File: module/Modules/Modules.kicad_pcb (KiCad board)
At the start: 2 copper layers, 165.5 x 77.7 mm, 27 parts, among them J1 Conn_01x04_MountingPin, J2 Conn_01x04, J3 Conn_01x04, J4 Conn_01x04, U1 COM-09032, U2 LTC4316xDD, U3 24LC32, U7 24AA02-OT, U9 ADS1115IDGS

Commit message: update
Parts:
- removed JP3: SolderJumper_3_Open, Jumper:SolderJumper-3_P1.3mm_Open_RoundedPad1.0x1.5mm_NumberLabels
- removed R2, R4: R, PCM_Resistor_SMD_AKL:R_0805_2012Metric_Pad1.15x1.40mm_HandSolder
- removed U2: LTC4316xDD, Package_SO:MSOP-10_3x3mm_P0.5mm
- removed U3: 24LC32, Package_SO:SOIC-8_3.9x4.9mm_P1.27mm
- added J1: Conn_01x04_MountingPin, Connector_JST:JST_SH_BM04B-SRSS-TB_1x04-1MP_P1.00mm_Vertical, F.Cu at (253.9, 111.3)
- added JP2: int, Jumper:SolderJumper-2_P1.3mm_Open_RoundedPad1.0x1.5mm, B.Cu at (262.6, 89.3)
- JP1: value SolderJumper_3_Open -> WP; footprint Jumper:SolderJumper-3_P1.3mm_Open_RoundedPad1.0x1.5mm_NumberLabels -> Jumper:SolderJumper-2_P1.3mm_Open_RoundedPad1.0x1.5mm; moved to B.Cu
- R1: value R -> 100k
- R3: value R -> 100k; moved to B.Cu
- moved U7 36.0 mm to (238.4, 102.9), turned to 90 degrees
- moved JP1 23.0 mm to (262.4, 95.5), turned to 90 degrees
- moved R3 21.8 mm to (262.6, 99.9), turned to 90 degrees
- moved R1 15.5 mm to (251.8, 86.0), turned to 90 degrees
- moved J1 3.75 mm to (246.1, 111.3)
- moved J2 0.38 mm to (253.8, 107.3)
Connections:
- JP1 pad 1: Net-(JP1-A) -> /wp
- JP1 pad 2: /wp -> /Vdd
- R1 pad 1: Net-(JP3-A) -> /Gnd
- R1 pad 2: /Gnd -> /int
- R3 pad 1: Net-(JP1-A) -> /Gnd
- R3 pad 2: /Gnd -> /wp
- U7 pad 1: unconnected-(U7-SCL-Pad1) -> /SCL
- U7 pad 2: unconnected-(U7-V_{SS}-Pad2) -> /Gnd
- U7 pad 3: unconnected-(U7-SDA-Pad3) -> /SDA
- U7 pad 4: unconnected-(U7-V_{CC}-Pad4) -> /Vdd
- U7 pad 5: unconnected-(U7-WP-Pad5) -> /wp

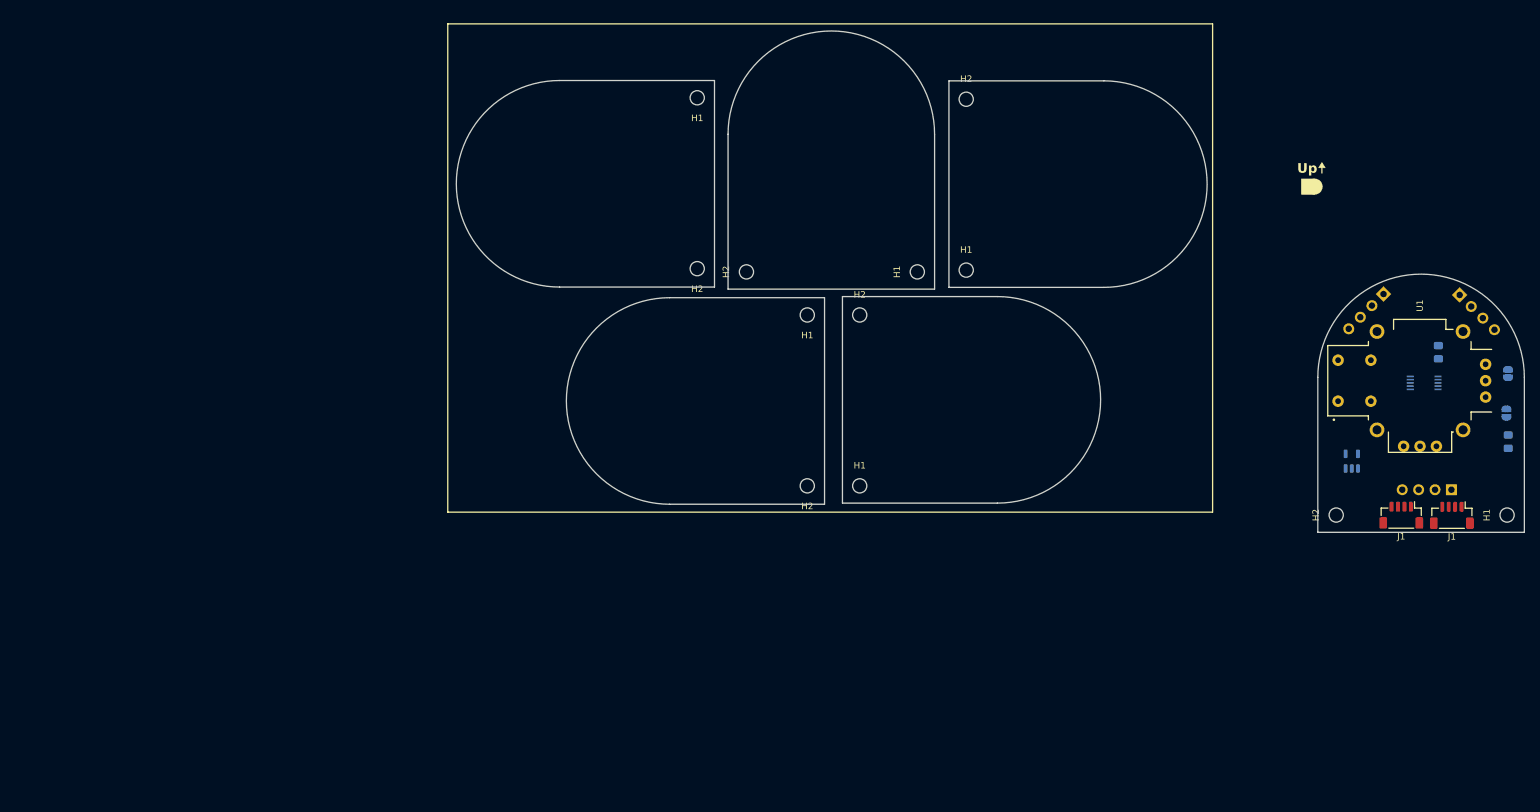
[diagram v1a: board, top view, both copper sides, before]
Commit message: module spec update
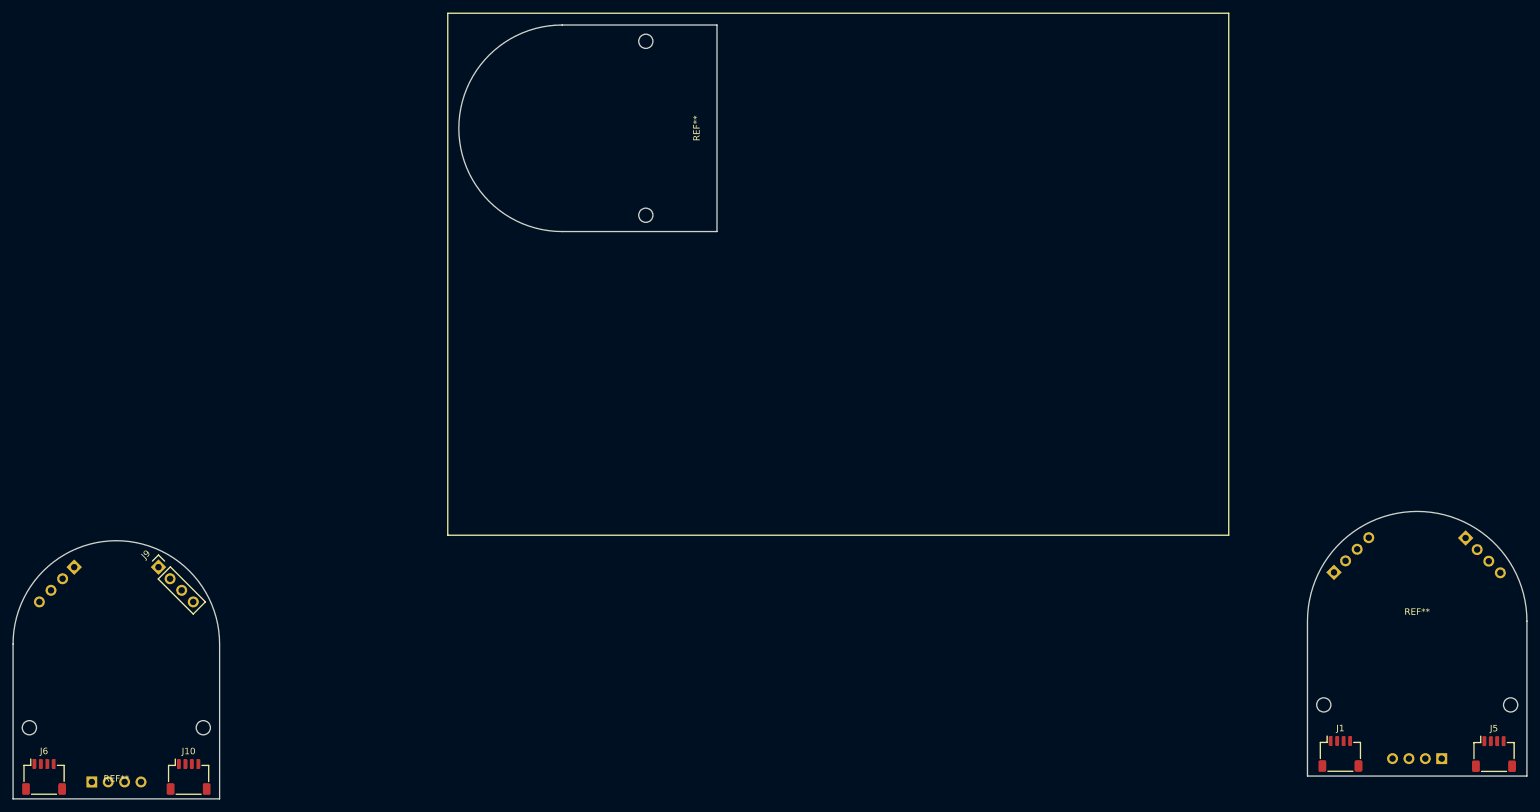
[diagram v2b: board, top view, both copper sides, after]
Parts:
- removed H1 (x6), H2 (x6): MountingHole, MountingHole:MountingHole_2.2mm_M2
- removed the J1 at (253.9, 111.3)
- removed JP1: WP, Jumper:SolderJumper-2_P1.3mm_Open_RoundedPad1.0x1.5mm
- removed JP2: int, Jumper:SolderJumper-2_P1.3mm_Open_RoundedPad1.0x1.5mm
- removed R1, R3: 100k, PCM_Resistor_SMD_AKL:R_0805_2012Metric_Pad1.15x1.40mm_HandSolder
- removed U1: COM-09032, COM_09032:XDCR_COM-09032
- removed U7: 24AA02-OT, Package_TO_SOT_SMD:SOT-23-5
- removed U9: ADS1115IDGS, Package_SO:TSSOP-10_3x3mm_P0.5mm
- added J10: JST SH, Connector_JST:JST_SH_SM04B-SRSS-TB_1x04-1MP_P1.00mm_Horizontal, F.Cu at (58.2, 151.8)
- added J5: JST SH, Connector_JST:JST_SH_SM04B-SRSS-TB_1x04-1MP_P1.00mm_Horizontal, F.Cu at (260.4, 148.3)
- added J6: JST SH, Connector_JST:JST_SH_SM04B-SRSS-TB_1x04-1MP_P1.00mm_Horizontal, F.Cu at (35.8, 151.8)
- added J7: Conn_01x04, Connector_PinSocket_2.54mm:PinSocket_1x04_P2.54mm_Vertical, B.Cu at (40.5, 119.3)
- added J8: Conn_01x04, Connector_PinSocket_2.54mm:PinSocket_1x04_P2.54mm_Vertical, B.Cu at (43.2, 152.6)
- added J9: Conn_01x04, Connector_PinSocket_2.54mm:PinSocket_1x04_P2.54mm_Vertical, F.Cu at (53.5, 119.3)
- added REF**: Module base, OSMC_Module:Module standard, F.Cu at (47.0, 152.6)
- added REF**: Module base, OSMC_Module:Module standard, F.Cu at (137.4, 51.4)
- added REF**: Module standard v2, OSMC_Module:Module standard v2, F.Cu at (248.6, 127.7)
- J1: value Conn_01x04_MountingPin -> JST SH; footprint Connector_JST:JST_SH_BM04B-SRSS-TB_1x04-1MP_P1.00mm_Vertical -> Connector_JST:JST_SH_SM04B-SRSS-TB_1x04-1MP_P1.00mm_Horizontal
- moved J3 43.8 mm to (235.7, 120.2), turned to -45 degrees
- moved J2 41.7 mm to (252.3, 149.0)
- moved J1 38.2 mm to (236.7, 148.3), turned to 0 degrees
- moved J4 37.7 mm to (256.0, 114.8)
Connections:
- J1 pad 1: /SCL -> /Gnd
- J1 pad 2: /SDA -> /Vdd
- J1 pad 3: /Vdd -> /SDA
- J1 pad 4: /Gnd -> /SCL
- J4 pad 1: /5V -> /Gnd
- J4 pad 2: /Gnd -> /5V
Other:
- board size 165.5 x 77.7 mm -> 34 x 41 mm
- board text added: "Large"
- board text added: "Small"
- board text removed: "Up"

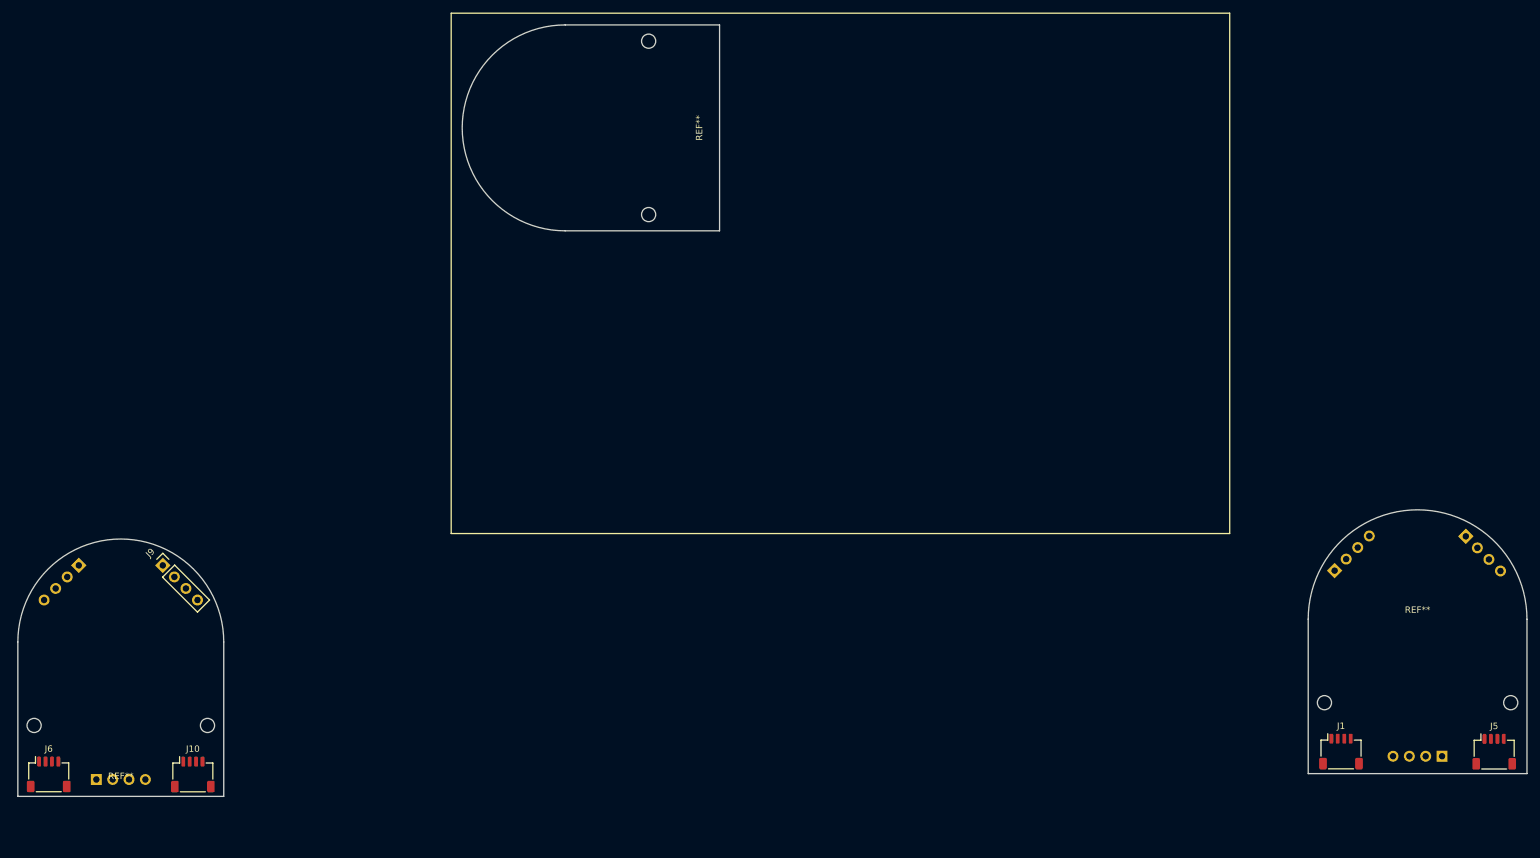
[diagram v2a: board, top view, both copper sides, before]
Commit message: updated templet and renamed lib files
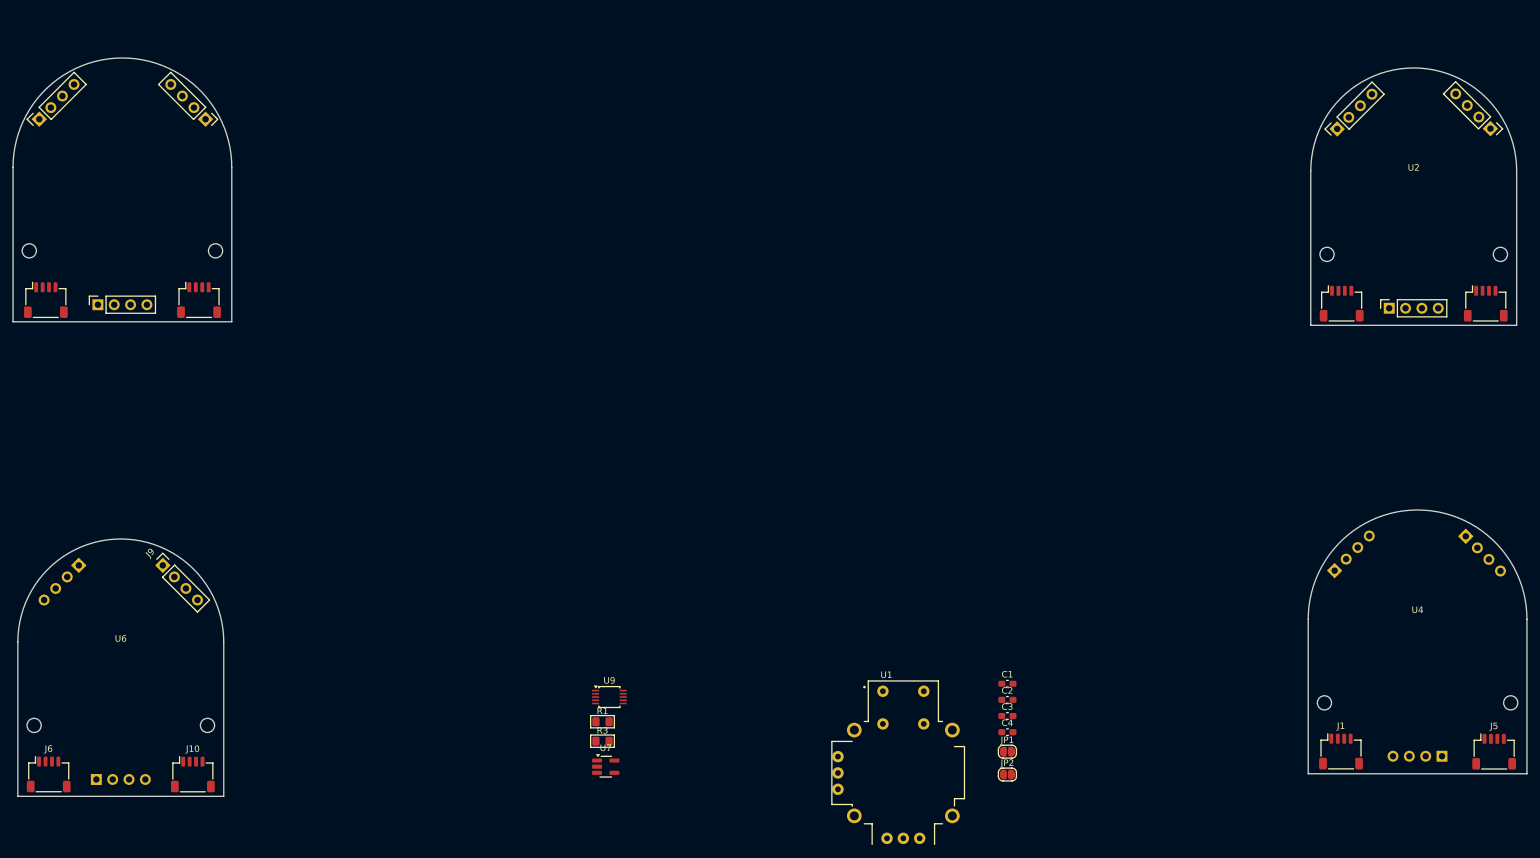
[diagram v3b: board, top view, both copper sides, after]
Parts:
- removed REF** (x2): Module base, OSMC_Module:Module standard
- removed REF**: Module standard v2, OSMC_Module:Module standard v2
- added C1: .1 u, Capacitor_SMD:C_0603_1608Metric_Pad1.08x0.95mm_HandSolder, F.Cu at (184.8, 137.7)
- added C2: 10 u, Capacitor_SMD:C_0603_1608Metric_Pad1.08x0.95mm_HandSolder, F.Cu at (184.8, 140.2)
- added C3: C, Capacitor_SMD:C_0603_1608Metric_Pad1.08x0.95mm_HandSolder, F.Cu at (184.8, 142.8)
- added C4: C, Capacitor_SMD:C_0603_1608Metric_Pad1.08x0.95mm_HandSolder, F.Cu at (184.8, 145.3)
- added JP1: WP, Jumper:SolderJumper-2_P1.3mm_Open_RoundedPad1.0x1.5mm, F.Cu at (184.8, 148.3)
- added JP2: int, Jumper:SolderJumper-2_P1.3mm_Open_RoundedPad1.0x1.5mm, F.Cu at (184.8, 151.8)
- added R1: 100k, PCM_Resistor_SMD_AKL:R_0805_2012Metric_Pad1.15x1.40mm_HandSolder, F.Cu at (121.9, 143.6)
- added R3: 100k, PCM_Resistor_SMD_AKL:R_0805_2012Metric_Pad1.15x1.40mm_HandSolder, F.Cu at (121.9, 146.7)
- added U1: COM-09032, COM_09032:XDCR_COM-09032, F.Cu at (168.6, 151.6)
- added U2: OSMC Module Board w/pins, OSMC_Module:Module standard pin, F.Cu at (247.9, 58.0)
- added U4: OSMC Module Board, OSMC_Module:Module standard v2, F.Cu at (248.6, 127.7)
- added U5: OSMC Module Board w/pins, OSMC_Module:Module standard pin v2, F.Cu at (47.2, 57.5)
- added U6: OSMC Module Board, OSMC_Module:Module standard, F.Cu at (47.0, 152.6)
- added U7: 24AA02-OT, Package_TO_SOT_SMD:SOT-23-5_HandSoldering, F.Cu at (122.4, 150.6)
- added U9: ADS1115IDGS, Package_SO:TSSOP-10_3x3mm_P0.5mm, F.Cu at (122.9, 139.8)

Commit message: update
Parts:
- C2: value 10 u -> .1 u
- U2: footprint OSMC_Module:Module standard pin -> OSMC_Module:Module standard pin small
- U4: footprint OSMC_Module:Module standard v2 -> OSMC_Module:Module standard small
- U5: footprint OSMC_Module:Module standard pin v2 -> OSMC_Module:Module standard pin large
- U6: footprint OSMC_Module:Module standard -> OSMC_Module:Module standard large
- U7: footprint Package_TO_SOT_SMD:SOT-23-5_HandSoldering -> Package_TO_SOT_SMD:SOT-23-5
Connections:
- U2 pad 1: Net-(U2-Gnd-Pad1) -> Net-(U2-GND)
- U2 pad 10: Net-(U2-NC-Pad10) -> Net-(U2-5V-Pad10)
- U2 pad 11: (no net) -> Net-(U2-OPT-Pad11)
- U2 pad 12: unconnected-(U2-Int-Pad12) -> Net-(U2-Int-Pad12)
- U2 pad 13: unconnected-(U2-A1-Pad13) -> Net-(U2-Int-Pad12)
- U2 pad 14: unconnected-(U2-A2-Pad14) -> Net-(U2-OPT-Pad11)
- U2 pad 15: unconnected-(U2-A3-Pad15) -> Net-(U2-5V-Pad10)
- U2 pad 16: Net-(U2-NC-Pad10) -> Net-(U2-GND)
- U2 pad 17: (no net) -> unconnected-(U2-NC-Pad17)
- U2 pad 18: (no net) -> unconnected-(U2-A3-Pad18)
- U2 pad 19: (no net) -> unconnected-(U2-A2-Pad19)
- U2 pad 20: (no net) -> unconnected-(U2-A1-Pad20)
- U2 pad 5: Net-(U2-Gnd-Pad1) -> Net-(U2-GND)
- U2 pad 9: Net-(U2-Gnd-Pad1) -> Net-(U2-GND)
- U5 pad 10: Net-(U5-NC-Pad10) -> Net-(U5-5V-Pad15)
- U5 pad 11: (no net) -> Net-(U5-OPT-Pad11)
- U5 pad 12: unconnected-(U5-Int-Pad12) -> Net-(U5-Int-Pad12)
- U5 pad 13: unconnected-(U5-A1-Pad13) -> Net-(U5-Int-Pad12)
- U5 pad 14: unconnected-(U5-A2-Pad14) -> Net-(U5-OPT-Pad11)
- U5 pad 15: unconnected-(U5-A3-Pad15) -> Net-(U5-5V-Pad15)
- U5 pad 16: Net-(U5-NC-Pad10) -> Net-(U5-Gnd-Pad1)
- U5 pad 17: (no net) -> unconnected-(U5-NC-Pad17)
- U5 pad 18: (no net) -> unconnected-(U5-A3-Pad18)
- U5 pad 19: (no net) -> unconnected-(U5-A2-Pad19)
- U5 pad 20: (no net) -> unconnected-(U5-A1-Pad20)

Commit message: update
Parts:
- added R10: 10k, OSMC_parts:R_0805_2012Metric_Pad1.15x1.40mm_HandSolder, F.Cu at (120.7, 110.3)
- added R11: 10k, OSMC_parts:R_0805_2012Metric_Pad1.15x1.40mm_HandSolder, F.Cu at (120.7, 113.3)
- added R13: 10k, OSMC_parts:R_0805_2012Metric_Pad1.15x1.40mm_HandSolder, F.Cu at (125.5, 101.2)
- added R14: 10k, OSMC_parts:R_0805_2012Metric_Pad1.15x1.40mm_HandSolder, F.Cu at (125.5, 104.2)
- added R16: 10k, OSMC_parts:R_0805_2012Metric_Pad1.15x1.40mm_HandSolder, F.Cu at (125.5, 107.2)
- added R17: 10k, OSMC_parts:R_0805_2012Metric_Pad1.15x1.40mm_HandSolder, F.Cu at (125.5, 110.3)
- added R18: 10k, OSMC_parts:R_0805_2012Metric_Pad1.15x1.40mm_HandSolder, F.Cu at (125.5, 113.3)
- added R7: 10k, OSMC_parts:R_0805_2012Metric_Pad1.15x1.40mm_HandSolder, F.Cu at (120.7, 101.2)
- added R8: 10k, OSMC_parts:R_0805_2012Metric_Pad1.15x1.40mm_HandSolder, F.Cu at (120.7, 104.2)
- added R9: 10k, OSMC_parts:R_0805_2012Metric_Pad1.15x1.40mm_HandSolder, F.Cu at (120.7, 107.2)
- added U10: LTC4317, OSMC_parts:DFN-16-1EP_3x5mm_P0.5mm_EP1.66x4.4mm, F.Cu at (130.9, 103.0)
- added U11: XIAO-ESP32-S3-DIP, OSMC_parts:XIAO-ESP32-S3-DIP, F.Cu at (160.5, 91.9)
- added U8: PCF8574DWR, OSMC_parts:DW16-L, F.Cu at (155.7, 108.0)
- C1, C2, C3, C4: footprint Capacitor_SMD:C_0603_1608Metric_Pad1.08x0.95mm_HandSolder -> OSMC_parts:C_0603_1608Metric_Pad1.08x0.95mm_HandSolder
- J1, J10, J5, J6: footprint Connector_JST:JST_SH_SM04B-SRSS-TB_1x04-1MP_P1.00mm_Horizontal -> OSMC_parts:JST_SH_SM04B-SRSS-TB_1x04-1MP_P1.00mm_Horizontal
- J2, J3, J4, J7, J8, J9: footprint Connector_PinSocket_2.54mm:PinSocket_1x04_P2.54mm_Vertical -> OSMC_parts:PinSocket_1x04_P2.54mm_Vertical
- JP1: footprint Jumper:SolderJumper-2_P1.3mm_Open_RoundedPad1.0x1.5mm -> OSMC_parts:SolderJumper-2_P1.3mm_Open_RoundedPad1.0x1.5mm
- JP2: value int -> Det; footprint Jumper:SolderJumper-2_P1.3mm_Open_RoundedPad1.0x1.5mm -> OSMC_parts:SolderJumper-2_P1.3mm_Open_RoundedPad1.0x1.5mm
- R1, R3: footprint PCM_Resistor_SMD_AKL:R_0805_2012Metric_Pad1.15x1.40mm_HandSolder -> OSMC_parts:R_0805_2012Metric_Pad1.15x1.40mm_HandSolder
- U1: footprint COM_09032:XDCR_COM-09032 -> OSMC_parts:XDCR_COM-09032
- U2: footprint OSMC_Module:Module standard pin small -> OSMC_parts:Module standard pin large
- U4: footprint OSMC_Module:Module standard small -> OSMC_parts:Module standard large
- U5: footprint OSMC_Module:Module standard pin large -> OSMC_parts:Module standard pin small
- U6: footprint OSMC_Module:Module standard large -> OSMC_parts:Module standard small
- U7: footprint Package_TO_SOT_SMD:SOT-23-5 -> OSMC_parts:SOT-23-5
- U9: footprint Package_SO:TSSOP-10_3x3mm_P0.5mm -> OSMC_parts:TSSOP-10_3x3mm_P0.5mm
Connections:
- J3 pad 2: /I03 -> /Gnd
- J3 pad 3: /IO2 -> /Gnd
- J3 pad 4: /IO1 -> /Gnd
- J4 pad 3: unconnected-(J4-Pin_3-Pad3) -> /Opt
- J4 pad 4: /int -> /Det
- J7 pad 2: /I03 -> /Gnd
- J7 pad 3: /IO2 -> /Gnd
- J7 pad 4: /IO1 -> /Gnd
- J9 pad 3: unconnected-(J9-Pin_3-Pad3) -> /Opt
- J9 pad 4: /int -> /Det
- JP2 pad 1: /int -> /Det
- R1 pad 2: /int -> /Det
- U9 pad 2: unconnected-(U9-ALERT/RDY-Pad2) -> /int

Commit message: update
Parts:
- added J11: JST SH, OSMC_parts:PinSocket_1x04_P2.54mm_Vertical, F.Cu at (101.9, 66.0)
- added J12: Conn_01x08_Socket, OSMC_parts:Button Spacing, F.Cu at (47.3, 57.5)
- added R12: 10k, OSMC_parts:R_0805_2012Metric_Pad1.15x1.40mm_HandSolder, F.Cu at (97.2, 77.3)
- added R15: 10k, OSMC_parts:R_0805_2012Metric_Pad1.15x1.40mm_HandSolder, F.Cu at (97.2, 80.3)
- added R19: 10k, OSMC_parts:R_0805_2012Metric_Pad1.15x1.40mm_HandSolder, F.Cu at (97.2, 83.3)
- added R2: 100k, OSMC_parts:R_0805_2012Metric_Pad1.15x1.40mm_HandSolder, F.Cu at (97.2, 65.2)
- added R20: 10k, OSMC_parts:R_0805_2012Metric_Pad1.15x1.40mm_HandSolder, F.Cu at (97.2, 86.3)
- added R4: 100k, OSMC_parts:R_0805_2012Metric_Pad1.15x1.40mm_HandSolder, F.Cu at (97.2, 68.2)
- added R5: 100k, OSMC_parts:R_0805_2012Metric_Pad1.15x1.40mm_HandSolder, F.Cu at (97.2, 71.2)
- added R6: 100k, OSMC_parts:R_0805_2012Metric_Pad1.15x1.40mm_HandSolder, F.Cu at (97.2, 74.2)
- added SW1: SW_Push, OSMC_parts:Membrane Button semi 4 mm, F.Cu at (69.0, 41.5)
- J2, J3, J4, J7, J8, J9: footprint OSMC_parts:PinSocket_1x04_P2.54mm_Vertical -> Connector_JST:JST_SH_BM04B-SRSS-TB_1x04-1MP_P1.00mm_Vertical
- U10: footprint OSMC_parts:DFN-16-1EP_3x5mm_P0.5mm_EP1.66x4.4mm -> OSMC_parts:TSSOP-10_3x3mm_P0.5mm
- U2: footprint OSMC_parts:Module standard pin large -> OSMC_parts:Module standard pin small
- U4: footprint OSMC_parts:Module standard large -> OSMC_parts:DFN-16-1EP_3x5mm_P0.5mm_EP1.66x4.4mm
- U5: footprint OSMC_parts:Module standard pin small -> OSMC_parts:Module standard large
- U6: footprint OSMC_parts:Module standard small -> OSMC_parts:Module standard pin large
